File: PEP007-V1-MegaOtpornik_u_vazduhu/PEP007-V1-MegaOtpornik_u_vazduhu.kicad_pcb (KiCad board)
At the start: 2 copper layers, 45 x 45 mm, 9 parts, among them J1 Screw_Terminal_01x02

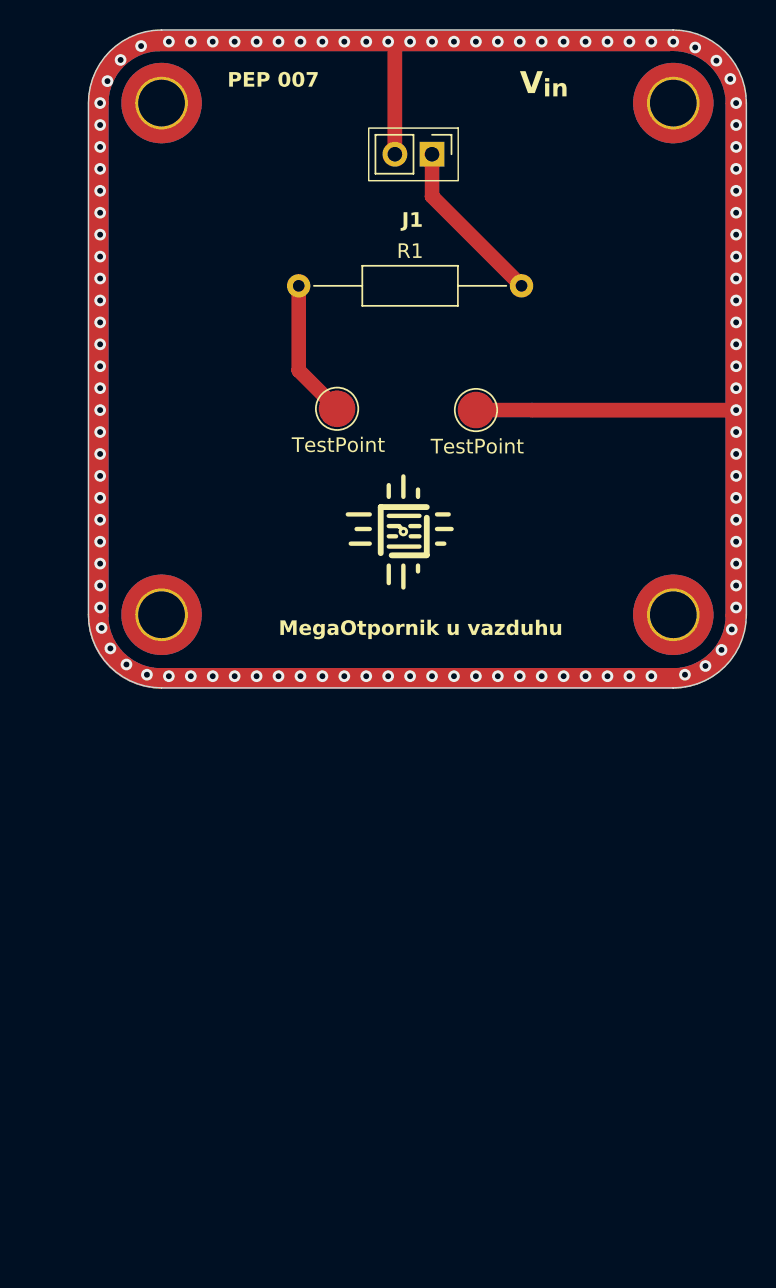
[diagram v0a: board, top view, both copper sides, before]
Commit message: Template, library and PEP7 update.
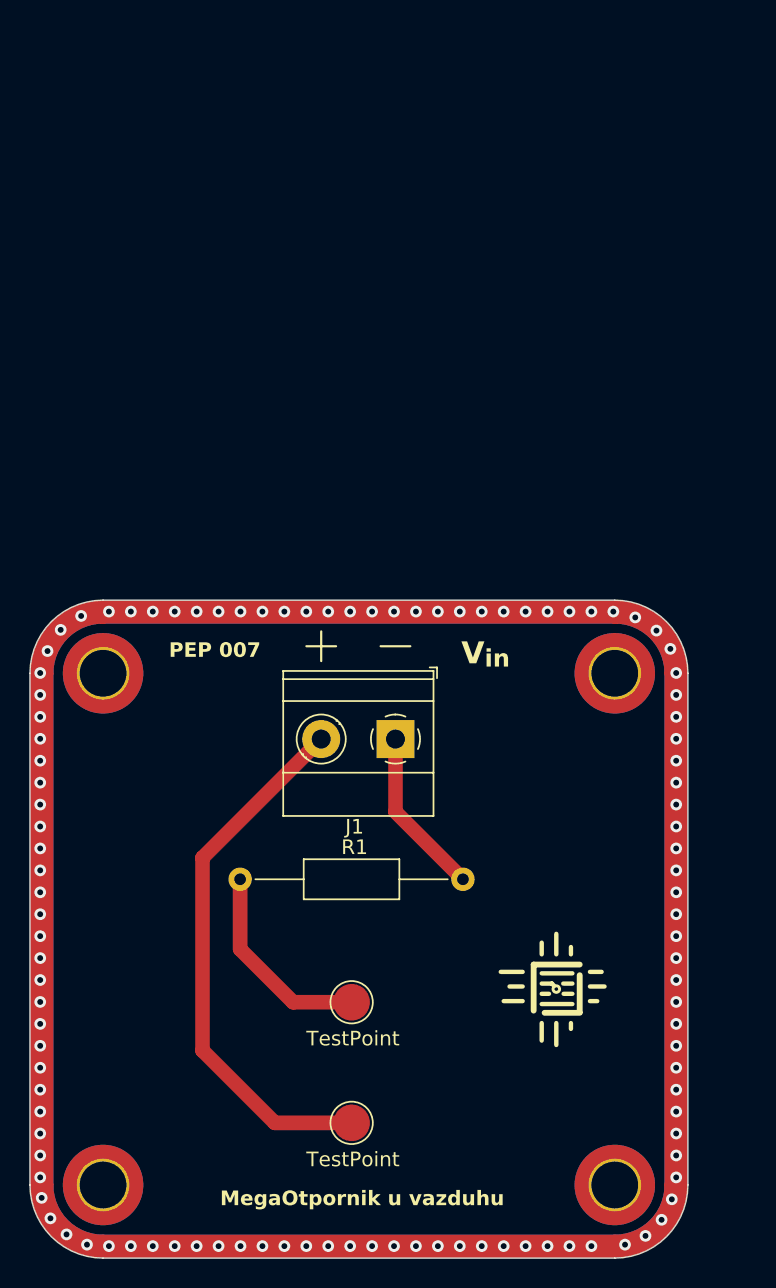
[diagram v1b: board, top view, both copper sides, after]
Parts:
- J1: footprint PEP_library:JP_Connector_PinHeader_2.54mmPinHeader_1x02_P2.54mm_Vertical -> PEP_library:TerminalBlock_Phoenix_MKDS-1,5-2-5.08_1x02_P5.08mm_Horizontal
- moved TP2 49.5 mm to (122.0, 135.8)
- moved R1 40.8 mm to (114.4, 119.1)
- moved TP2 40.6 mm to (122.0, 127.5)
- moved J1 40.0 mm to (125.0, 109.5), turned to 180 degrees
- moved H1 39.2 mm to (105.0, 140.0)
- moved H2 39.2 mm to (105.0, 105.0)
- moved H3 39.2 mm to (140.0, 105.0)
- moved H4 39.2 mm to (140.0, 140.0)
- moved REF** 33.0 mm to (136.0, 126.6)
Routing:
- net 0: track 25.7 -> 36.9 mm, vias 109 -> 0
- net Net-(R1-Pad1): track 9.50 -> 13.9 mm
- net (no net): vias 0 -> 109

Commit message: PEP007 and lib update.
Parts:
- removed J1: Screw_Terminal_01x02, PEP_library:TerminalBlock_Phoenix_MKDS-1,5-2-5.08_1x02_P5.08mm_Horizontal
- added J2: Klema, PEP_library:TerminalBlock_Phoenix_MKDS-1,5-2-5.08_1x02_P5.08mm_Horizontal, F.Cu at (119.9, 109.5)
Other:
- board text removed: "V_{in}"

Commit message: Update 1,2,3,4,5,7, lib.
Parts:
- removed J2: Klema, PEP_library:TerminalBlock_Phoenix_MKDS-1,5-2-5.08_1x02_P5.08mm_Horizontal
- added J1: Klema, PEP_library:TerminalBlock_Phoenix_MKDS-1,5-2-5.08_1x02_P5.08mm_Horizontal, F.Cu at (125.0, 109.9)
- added REF**: LOGO, PEP_library:petnica_logo, F.Cu at (118.2, 125.8)
- TP2: value TestPoint -> TP2
- TP2: value TestPoint -> TP1
- moved R1 21.7 mm to (135.2, 125.1), turned to 90 degrees
- moved TP2 13.5 mm to (135.2, 132.9), turned to -90 degrees
- moved TP2 13.2 mm to (110.0, 133.0), turned to -90 degrees
- moved REF** 8.29 mm to (127.8, 125.8)
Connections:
- TP2 pad 1: Net-(R1-Pad1) -> 0
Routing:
- net Net-(R1-Pad1): track 13.9 -> 6.88 mm
- net 0: track 36.9 -> 33.1 mm
- net Input voltage: track 11.5 -> 9.81 mm
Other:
- board text added: "MegaOtpornik"
- board text removed: "MegaOtpornik u vazduhu"
- board text removed: "TestPoint"
